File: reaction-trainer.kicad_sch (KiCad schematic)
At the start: 0 parts

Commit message: Preliminary schematic modules
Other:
- added sheet CH32V208W (ch32V208w.kicad_sch)
- added sheet LED (led.kicad_sch)
- added sheet Motion (motion.kicad_sch)
- added sheet Power (power.kicad_sch)
- added sheet USB (usb.kicad_sch)
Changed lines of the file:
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@@
     (comment 1 "Released under CERN-OHL-P (see LICENSE)")
+  )
+  (sheet (at 78.74 22.86) (size 39.37 38.1) (fields_autoplaced)
+    (stroke (width 0.1524) (type solid))
+    (fill (color 0 0 0 0.0000))
+    (property "Sheetname" "Power" (at 78.74 22.1484 0)
+      (effects (font (size 1.27 1.27)) (justify left bottom))
+    )
+    (property "Sheetfile" "power.kicad_sch" (at 78.74 61.5446 0)
+      (effects (font (size 1.27 1.27)) (justify left top))
+    )
+    (instances
+      (project "reaction-trainer"
+        (path "/726cb70d-0185-4970-973b-037545fc3942" (page "3"))
+      )
+    )
+  )
+  (sheet (at 134.62 22.86) (size 40.64 38.1) (fields_autoplaced)
+    (stroke (width 0.1524) (type solid))
+    (fill (color 0 0 0 0.0000))
+    (property "Sheetname" "LED" (at 134.62 22.1484 0)
+      (effects (font (size 1.27 1.27)) (justify left bottom))
+    )
+    (property "Sheetfile" "led.kicad_sch" (at 134.62 61.5446 0)
+      (effects (font (size 1.27 1.27)) (justify left top))
+    )
+    (instances
+      (project "reaction-trainer"
+        (path "/726cb70d-0185-4970-973b-037545fc3942" (page "4"))
+      )
+    )
+  )
+  (sheet (at 190.5 22.86) (size 35.56 38.1) (fields_autoplaced)
+    (stroke (width 0.1524) (type solid))
+    (fill (color 0 0 0 0.0000))
+    (property "Sheetname" "Motion" (at 190.5 22.1484 0)
+      (effects (font (size 1.27 1.27)) (justify left bottom))
+    )
+    (property "Sheetfile" "motion.kicad_sch" (at 190.5 61.5446 0)
+      (effects (font (size 1.27 1.27)) (justify left top))
+    )
+    (instances
+      (project "reaction-trainer"
+        (path "/726cb70d-0185-4970-973b-037545fc3942" (page "5"))
+      )
+    )
+  )
+  (sheet (at 22.86 76.2) (size 45.72 39.37) (fields_autoplaced)
+    (stroke (width 0.1524) (type solid))
+    (fill (color 0 0 0 0.0000))
+    (property "Sheetname" "USB" (at 22.86 75.4884 0)
+      (effects (font (size 1.27 1.27)) (justify left bottom))
+    )
+    (property "Sheetfile" "usb.kicad_sch" (at 22.86 116.1546 0)
+      (effects (font (size 1.27 1.27)) (justify left top))
+    )
+    (instances
+      (project "reaction-trainer"
+        (path "/726cb70d-0185-4970-973b-037545fc3942" (page "6"))
+      )
+    )
+  )
+  (sheet (at 22.86 22.86) (size 45.72 38.1) (fields_autoplaced)
+    (stroke (width 0.1524) (type solid))
+    (fill (color 0 0 0 0.0000))
+    (property "Sheetname" "CH32V208W" (at 22.86 22.1484 0)
+      (effects (font (size 1.27 1.27)) (justify left bottom))
+    )
+    (property "Sheetfile" "ch32V208w.kicad_sch" (at 22.86 61.5446 0)
+      (effects (font (size 1.27 1.27)) (justify left top))
+    )
+    (instances
+      (project "reaction-trainer"
+        (path "/726cb70d-0185-4970-973b-037545fc3942" (page "2"))
+      )
+    )
   )
   (sheet_instances

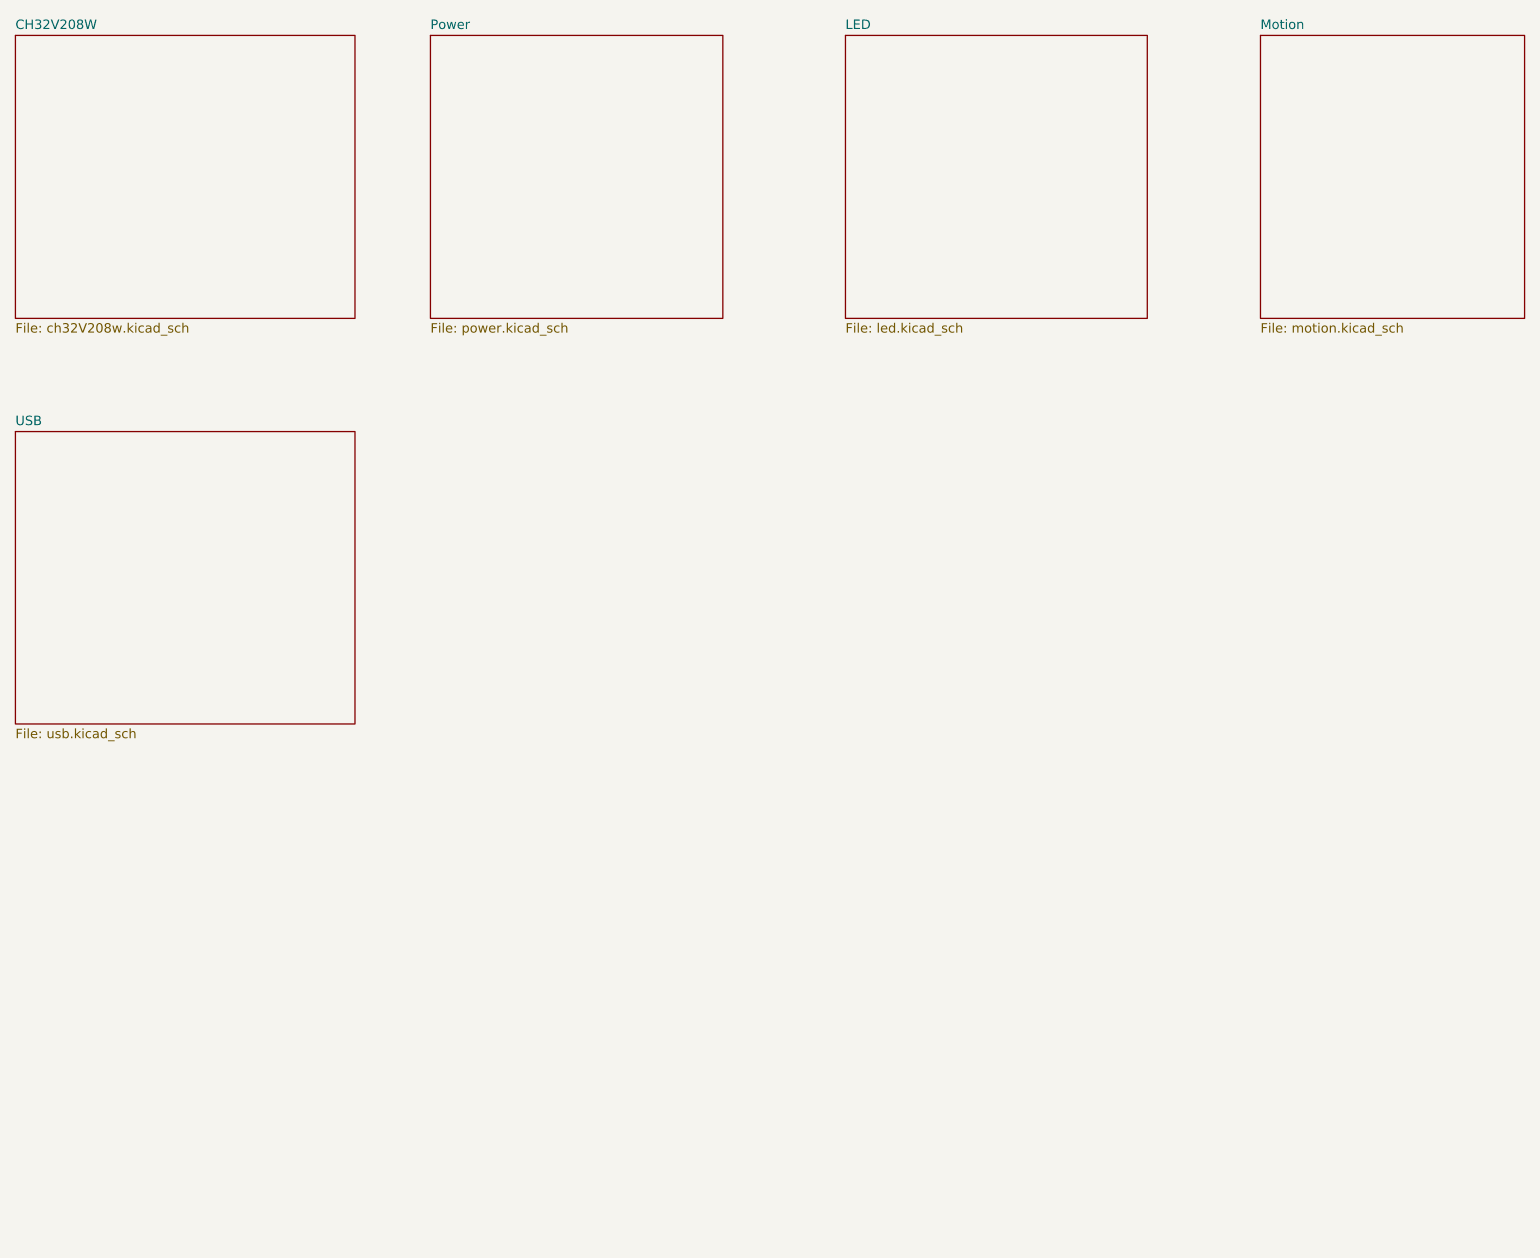
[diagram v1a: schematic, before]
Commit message: Added PWM audio out
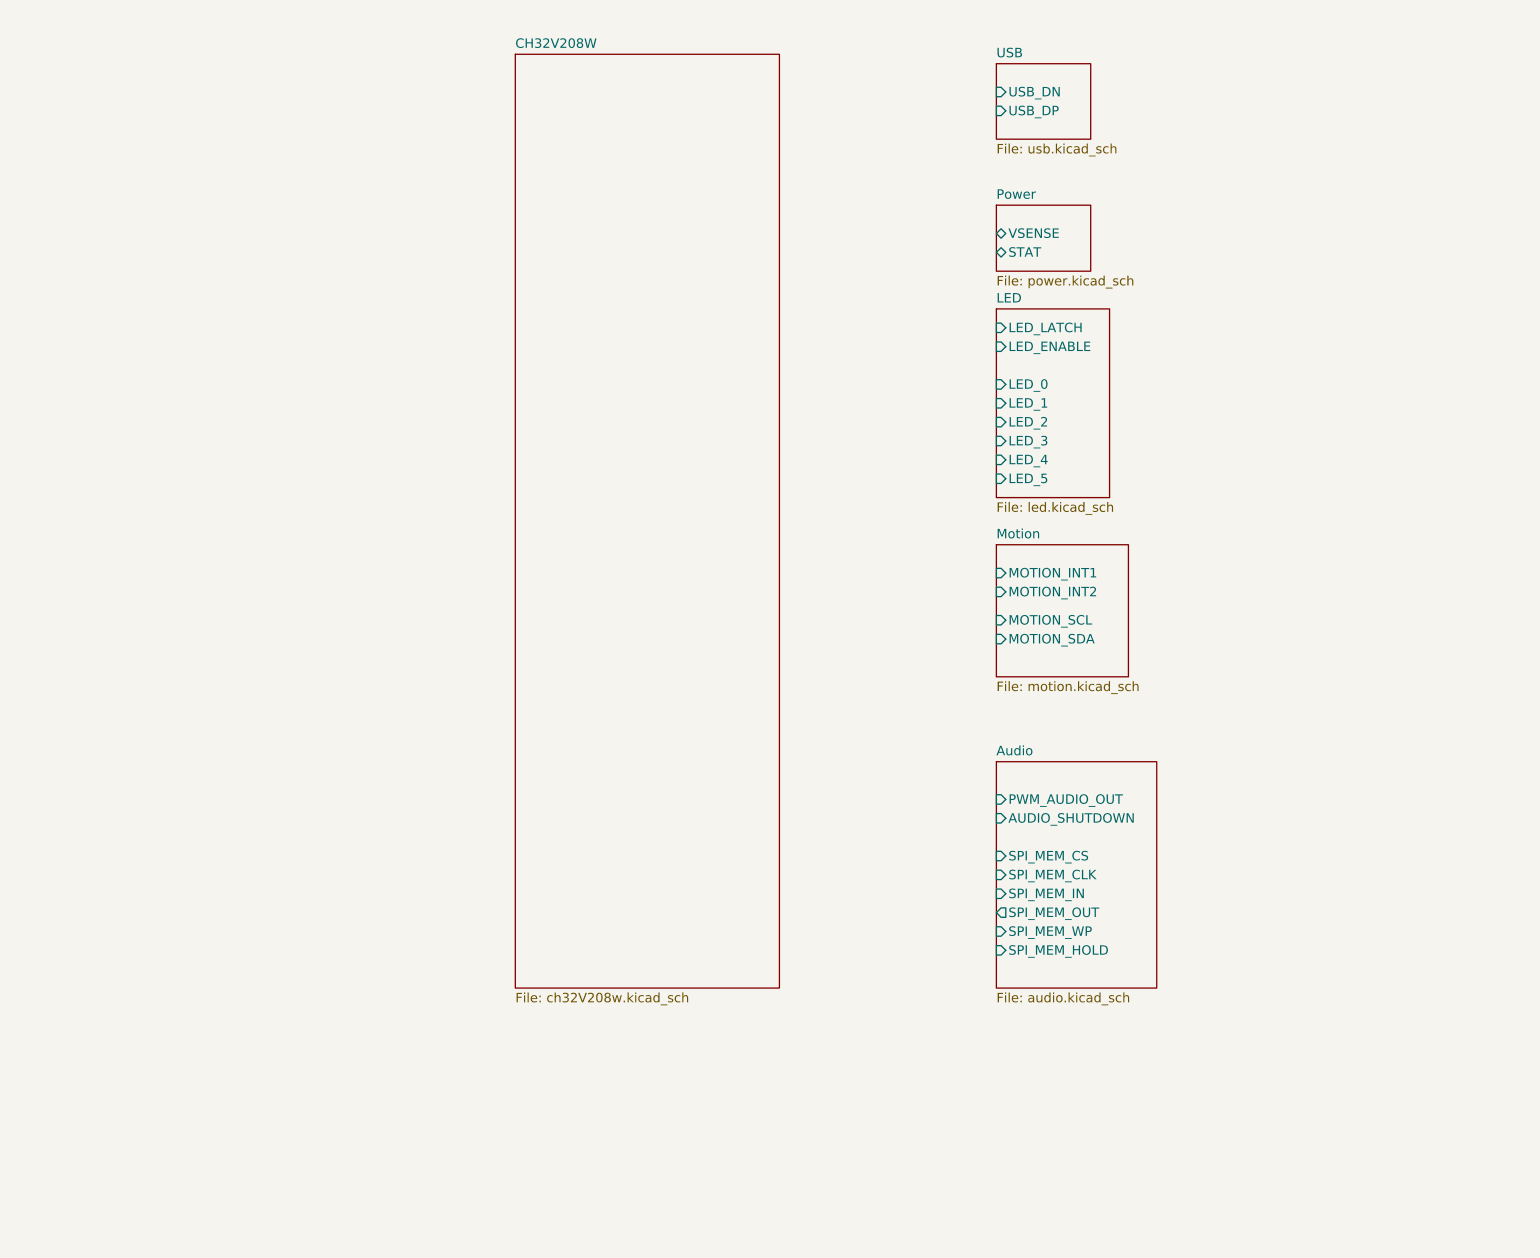
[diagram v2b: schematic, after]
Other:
- added sheet Audio (audio.kicad_sch)
- sheet LED ports: added LED_0, LED_1, LED_2, LED_3, LED_4, LED_5, LED_ENABLE, LED_LATCH; removed none
- sheet Motion ports: added MOTION_INT1, MOTION_INT2, MOTION_SCL, MOTION_SDA; removed none
- sheet Power ports: added STAT, VSENSE; removed none
- sheet USB ports: added USB_DN, USB_DP; removed none
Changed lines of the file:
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@@
     (comment 1 "Released under CERN-OHL-P (see LICENSE)")
   )
-  (sheet (at 78.74 22.86) (size 39.37 38.1) (fields_autoplaced)
+  (sheet (at 154.94 45.72) (size 12.7 8.89) (fields_autoplaced)
     (stroke (width 0.1524) (type solid))
     (fill (color 0 0 0 0.0000))
-    (property "Sheetname" "Power" (at 78.74 22.1484 0)
+    (property "Sheetname" "Power" (at 154.94 45.0084 0)
       (effects (font (size 1.27 1.27)) (justify left bottom))
     )
-    (property "Sheetfile" "power.kicad_sch" (at 78.74 61.5446 0)
+    (property "Sheetfile" "power.kicad_sch" (at 154.94 55.1946 0)
       (effects (font (size 1.27 1.27)) (justify left top))
+    )
+    (pin "VSENSE" bidirectional (at 154.94 49.53 180)
+      (effects (font (size 1.27 1.27)) (justify left))
+    )
+    (pin "STAT" bidirectional (at 154.94 52.07 180)
+      (effects (font (size 1.27 1.27)) (justify left))
     )
     (instances
@@
     )
   )
-  (sheet (at 134.62 22.86) (size 40.64 38.1) (fields_autoplaced)
+  (sheet (at 154.94 59.69) (size 15.24 25.4) (fields_autoplaced)
     (stroke (width 0.1524) (type solid))
     (fill (color 0 0 0 0.0000))
-    (property "Sheetname" "LED" (at 134.62 22.1484 0)
+    (property "Sheetname" "LED" (at 154.94 58.9784 0)
       (effects (font (size 1.27 1.27)) (justify left bottom))
     )
-    (property "Sheetfile" "led.kicad_sch" (at 134.62 61.5446 0)
+    (property "Sheetfile" "led.kicad_sch" (at 154.94 85.6746 0)
       (effects (font (size 1.27 1.27)) (justify left top))
+    )
+    (pin "LED_LATCH" input (at 154.94 62.23 180)
+      (effects (font (size 1.27 1.27)) (justify left))
+    )
+    (pin "LED_ENABLE" input (at 154.94 64.77 180)
+      (effects (font (size 1.27 1.27)) (justify left))
+    )
+    (pin "LED_2" input (at 154.94 74.93 180)
+      (effects (font (size 1.27 1.27)) (justify left))
+    )
+    (pin "LED_0" input (at 154.94 69.85 180)
+      (effects (font (size 1.27 1.27)) (justify left))
+    )
+    (pin "LED_5" input (at 154.94 82.55 180)
+      (effects (font (size 1.27 1.27)) (justify left))
+    )
+    (pin "LED_1" input (at 154.94 72.39 180)
+      (effects (font (size 1.27 1.27)) (justify left))
+    )
+    (pin "LED_3" input (at 154.94 77.47 180)
+      (effects (font (size 1.27 1.27)) (justify left))
+    )
+    (pin "LED_4" input (at 154.94 80.01 180)
+      (effects (font (size 1.27 1.27)) (justify left))
     )
     (instances
@@
     )
   )
-  (sheet (at 190.5 22.86) (size 35.56 38.1) (fields_autoplaced)
+  (sheet (at 154.94 91.44) (size 17.78 17.78) (fields_autoplaced)
     (stroke (width 0.1524) (type solid))
     (fill (color 0 0 0 0.0000))
-    (property "Sheetname" "Motion" (at 190.5 22.1484 0)
+    (property "Sheetname" "Motion" (at 154.94 90.7284 0)
       (effects (font (size 1.27 1.27)) (justify left bottom))
     )
-    (property "Sheetfile" "motion.kicad_sch" (at 190.5 61.5446 0)
+    (property "Sheetfile" "motion.kicad_sch" (at 154.94 109.8046 0)
       (effects (font (size 1.27 1.27)) (justify left top))
+    )
+    (pin "MOTION_INT1" input (at 154.94 95.25 180)
+      (effects (font (size 1.27 1.27)) (justify left))
+    )
+    (pin "MOTION_INT2" input (at 154.94 97.79 180)
+      (effects (font (size 1.27 1.27)) (justify left))
+    )
+    (pin "MOTION_SCL" input (at 154.94 101.6 180)
+      (effects (font (size 1.27 1.27)) (justify left))
+    )
+    (pin "MOTION_SDA" input (at 154.94 104.14 180)
+      (effects (font (size 1.27 1.27)) (justify left))
     )
     (instances
@@
     )
   )
-  (sheet (at 22.86 76.2) (size 45.72 39.37) (fields_autoplaced)
+  (sheet (at 154.94 26.67) (size 12.7 10.16) (fields_autoplaced)
     (stroke (width 0.1524) (type solid))
     (fill (color 0 0 0 0.0000))
-    (property "Sheetname" "USB" (at 22.86 75.4884 0)
+    (property "Sheetname" "USB" (at 154.94 25.9584 0)
       (effects (font (size 1.27 1.27)) (justify left bottom))
     )
-    (property "Sheetfile" "usb.kicad_sch" (at 22.86 116.1546 0)
+    (property "Sheetfile" "usb.kicad_sch" (at 154.94 37.4146 0)
       (effects (font (size 1.27 1.27)) (justify left top))
+    )
+    (pin "USB_DN" input (at 154.94 30.48 180)
+      (effects (font (size 1.27 1.27)) (justify left))
+    )
+    (pin "USB_DP" input (at 154.94 33.02 180)
+      (effects (font (size 1.27 1.27)) (justify left))
     )
     (instances
@@
     )
   )
-  (sheet (at 22.86 22.86) (size 45.72 38.1) (fields_autoplaced)
+  (sheet (at 154.94 120.65) (size 21.59 30.48) (fields_autoplaced)
     (stroke (width 0.1524) (type solid))
     (fill (color 0 0 0 0.0000))
-    (property "Sheetname" "CH32V208W" (at 22.86 22.1484 0)
+    (property "Sheetname" "Audio" (at 154.94 119.9384 0)
       (effects (font (size 1.27 1.27)) (justify left bottom))
     )
-    (property "Sheetfile" "ch32V208w.kicad_sch" (at 22.86 61.5446 0)
+    (property "Sheetfile" "audio.kicad_sch" (at 154.94 151.7146 0)
       (effects (font (size 1.27 1.27)) (justify left top))
     )
+    (pin "PWM_AUDIO_OUT" input (at 154.94 125.73 180)
+      (effects (font (size 1.27 1.27)) (justify left))
+    )
+    (pin "SPI_MEM_CS" input (at 154.94 133.35 180)
+      (effects (font (size 1.27 1.27)) (justify left))
+    )
+    (pin "SPI_MEM_CLK" input (at 154.94 135.89 180)
+      (effects (font (size 1.27 1.27)) (justify left))
+    )
+    (pin "SPI_MEM_IN" input (at 154.94 138.43 180)
+      (effects (font (size 1.27 1.27)) (justify left))
+    )
+    (pin "SPI_MEM_OUT" output (at 154.94 140.97 180)
+      (effects (font (size 1.27 1.27)) (justify left))
+    )
+    (pin "SPI_MEM_WP" input (at 154.94 143.51 180)
+      (effects (font (size 1.27 1.27)) (justify left))
+    )
+    (pin "SPI_MEM_HOLD" input (at 154.94 146.05 180)
+      (effects (font (size 1.27 1.27)) (justify left))
+    )
+    (pin "AUDIO_SHUTDOWN" input (at 154.94 128.27 180)
+      (effects (font (size 1.27 1.27)) (justify left))
+    )
+    (instances
+      (project "reaction-trainer"
+        (path "/726cb70d-0185-4970-973b-037545fc3942" (page "7"))
+      )
+    )
+  )
+  (sheet (at 90.17 25.4) (size 35.56 125.73) (fields_autoplaced)
+    (stroke (width 0.1524) (type solid))
+    (fill (color 0 0 0 0.0000))
+    (property "Sheetname" "CH32V208W" (at 90.17 24.6884 0)
+      (effects (font (size 1.27 1.27)) (justify left bottom))
+    )
+    (property "Sheetfile" "ch32V208w.kicad_sch" (at 90.17 151.7146 0)
+      (effects (font (size 1.27 1.27)) (justify left top))
+    )

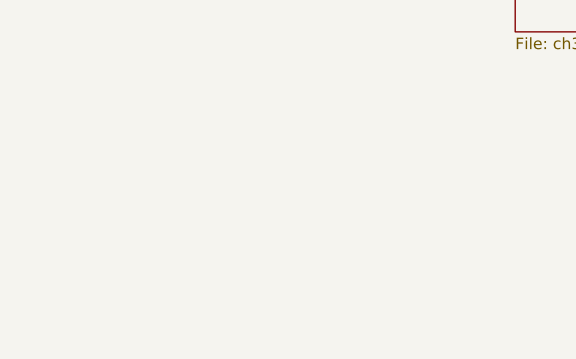
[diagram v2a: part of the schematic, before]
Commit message: Added Antenna design
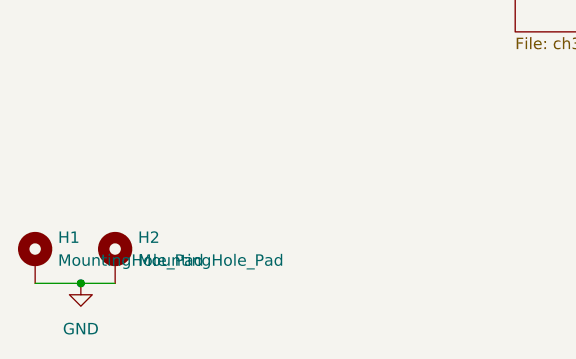
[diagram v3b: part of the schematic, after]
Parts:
- added H1, H2: MountingHole_Pad, MountingHole:MountingHole_3.2mm_M3_DIN965_Pad_TopBottom, symbol Mechanical:MountingHole_Pad
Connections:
- new net GND: H1.1, H2.1
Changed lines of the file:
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@@
     (comment 1 "Released under CERN-OHL-P (see LICENSE)")
+  )
+  (junction (at 41.91 179.07) (diameter 0) (color 0 0 0 0)
+  )
+  (wire (pts (xy 36.83 179.07) (xy 41.91 179.07))
+    (stroke (width 0) (type default))
+  )
+  (wire (pts (xy 41.91 179.07) (xy 45.72 179.07))
+    (stroke (width 0) (type default))
+  )
+  (symbol (lib_id "Mechanical:MountingHole_Pad") (at 45.72 176.53 0) (unit 1)
+    (in_bom yes) (on_board yes) (dnp no) (fields_autoplaced)
+    (property "Reference" "H2" (at 48.26 173.99 0)
+      (effects (font (size 1.27 1.27)) (justify left))
+    )
+    (property "Value" "MountingHole_Pad" (at 48.26 176.53 0)
+      (effects (font (size 1.27 1.27)) (justify left))
+    )
+    (property "Footprint" "MountingHole:MountingHole_3.2mm_M3_DIN965_Pad_TopBottom" (at 45.72 176.53 0)
+      (effects (font (size 1.27 1.27)) hide)
+    )
+    (property "Datasheet" "~" (at 45.72 176.53 0)
+      (effects (font (size 1.27 1.27)) hide)
+    )
+    (pin "1")
+    (instances
+      (project "reaction-trainer"
+        (path "/726cb70d-0185-4970-973b-037545fc3942"
+          (reference "H2") (unit 1)
+        )
+      )
+    )
+  )
+  (symbol (lib_id "Mechanical:MountingHole_Pad") (at 36.83 176.53 0) (unit 1)
+    (in_bom yes) (on_board yes) (dnp no) (fields_autoplaced)
+    (property "Reference" "H1" (at 39.37 173.99 0)
+      (effects (font (size 1.27 1.27)) (justify left))
+    )
+    (property "Value" "MountingHole_Pad" (at 39.37 176.53 0)
+      (effects (font (size 1.27 1.27)) (justify left))
+    )
+    (property "Footprint" "MountingHole:MountingHole_3.2mm_M3_DIN965_Pad_TopBottom" (at 36.83 176.53 0)
+      (effects (font (size 1.27 1.27)) hide)
+    )
+    (property "Datasheet" "~" (at 36.83 176.53 0)
+      (effects (font (size 1.27 1.27)) hide)
+    )
+    (pin "1")
+    (instances
+      (project "reaction-trainer"
+        (path "/726cb70d-0185-4970-973b-037545fc3942"
+          (reference "H1") (unit 1)
+        )
+      )
+    )
+  )
+  (symbol (lib_id "power:GND") (at 41.91 179.07 0) (unit 1)
+    (in_bom yes) (on_board yes) (dnp no) (fields_autoplaced)
+    (property "Reference" "#PWR066" (at 41.91 185.42 0)
+      (effects (font (size 1.27 1.27)) hide)
+    )
+    (property "Value" "GND" (at 41.91 184.15 0)
+      (effects (font (size 1.27 1.27)))
+    )
+    (property "Footprint" "" (at 41.91 179.07 0)
+      (effects (font (size 1.27 1.27)) hide)
+    )
+    (property "Datasheet" "" (at 41.91 179.07 0)
+      (effects (font (size 1.27 1.27)) hide)
+    )
+    (pin "1")
+    (instances
+      (project "reaction-trainer"
+        (path "/726cb70d-0185-4970-973b-037545fc3942"
+          (reference "#PWR066") (unit 1)
+        )
+      )
+    )
   )
   (sheet (at 154.94 45.72) (size 12.7 8.89) (fields_autoplaced)
